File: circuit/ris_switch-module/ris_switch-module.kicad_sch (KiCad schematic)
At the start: 32 parts, among them J1 JST-PH-5P-M, J12 JST-PH-5P-F, J13 JST-PH-5P-M, J14 JST-PH-2P-F, J15 JST-PH-2P-M, J2 JST-PH-5P-M, J3 JST-B2PS-VH-M, J4 JST-PH-2P-M, J5 JST-PH-2P-M, J6 JST-PH-2P-M, J7 JST-PH-2P-M, J8 JST-PH-2P-M, J9 JST-PH-2P-M, K1 SRD-03VDC-SL-C, K2 SRD-03VDC-SL-C, K3 SRD-03VDC-SL-C, K4 SRD-03VDC-SL-C, K5 SRD-03VDC-SL-C, K6 SRD-03VDC-SL-C, Q1 BC337-40, Q2 BC337-40, Q3 BC337-40, Q4 BC337-40, Q5 BC337-40, Q6 BC337-40, U5 74HC595N_112

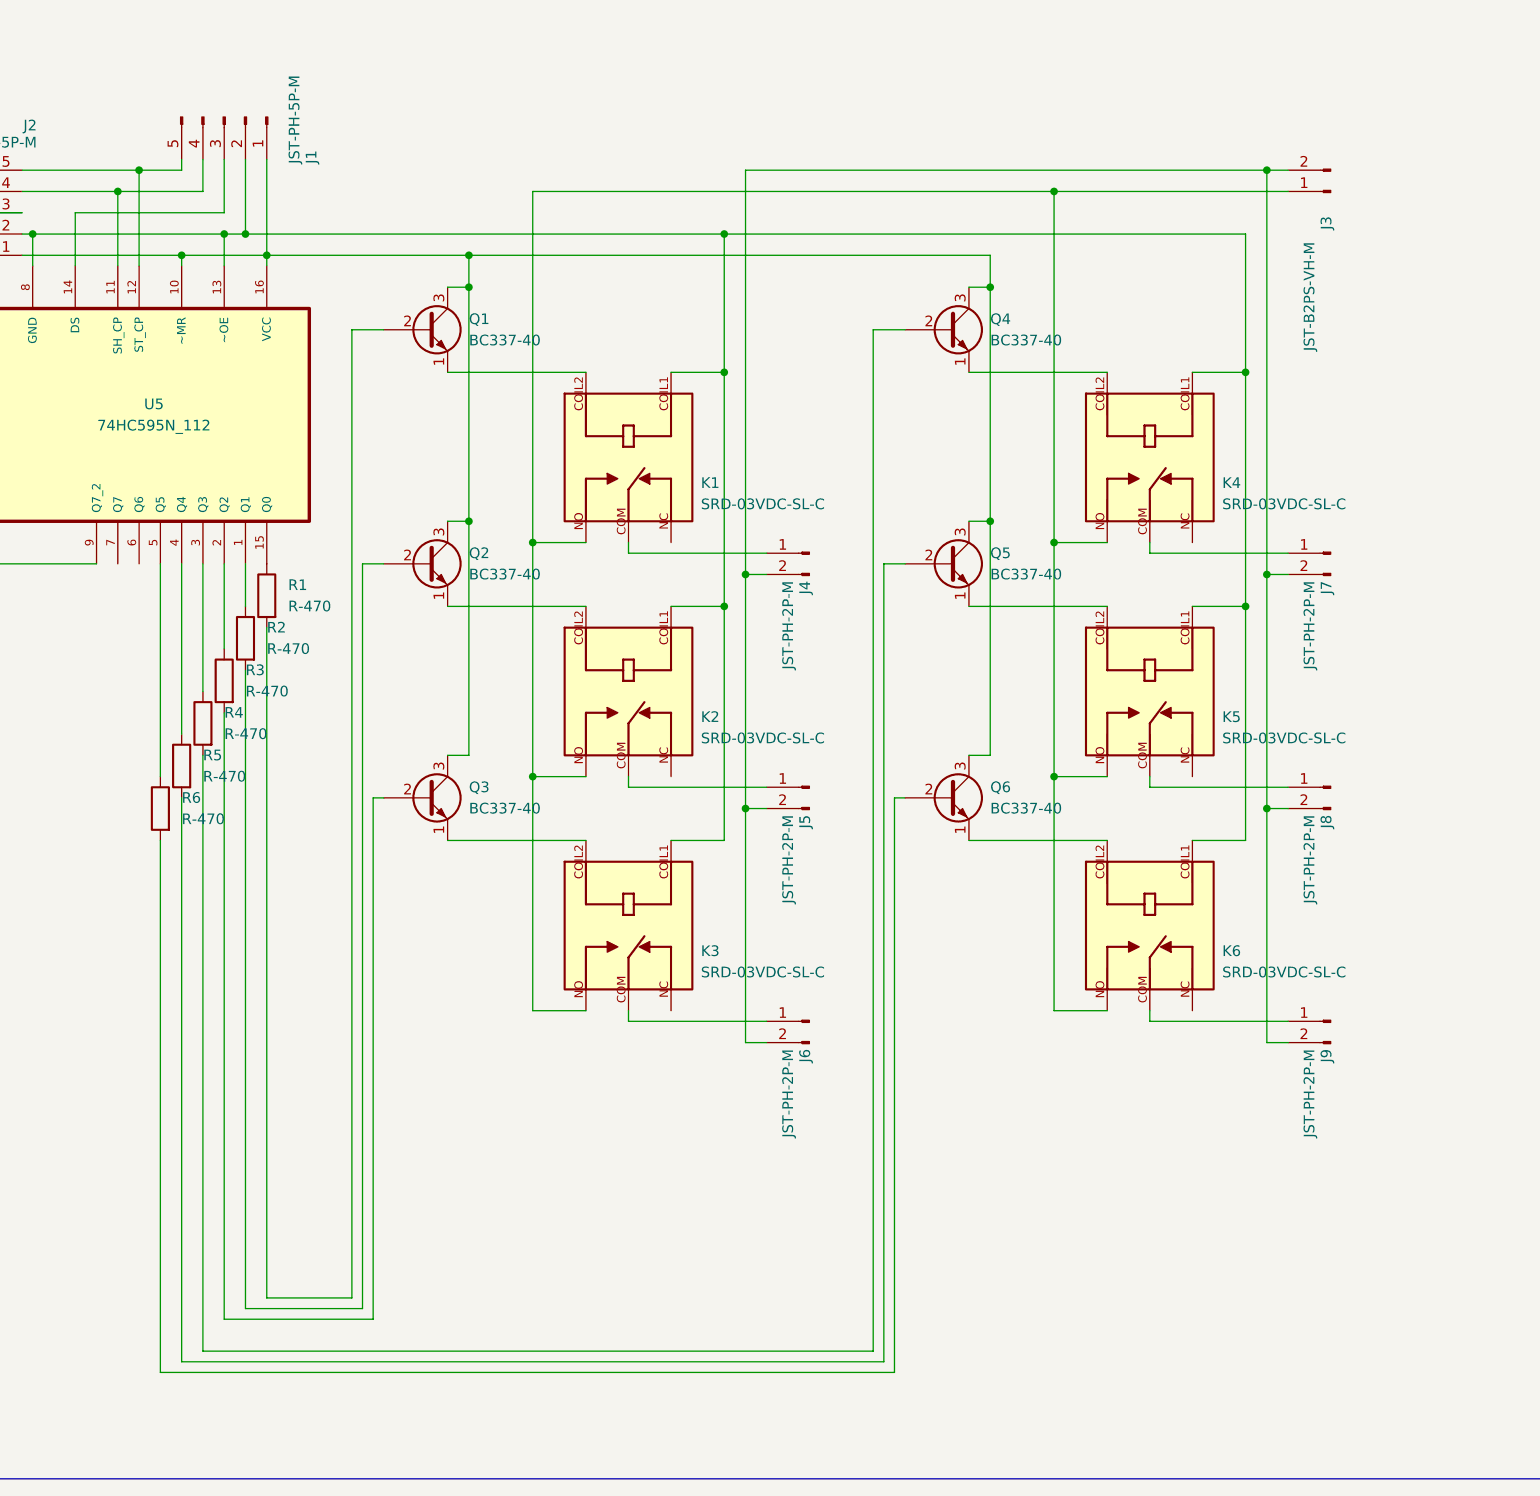
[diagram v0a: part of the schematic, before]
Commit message: Updated Circuit with Side Outputs & Mosfets
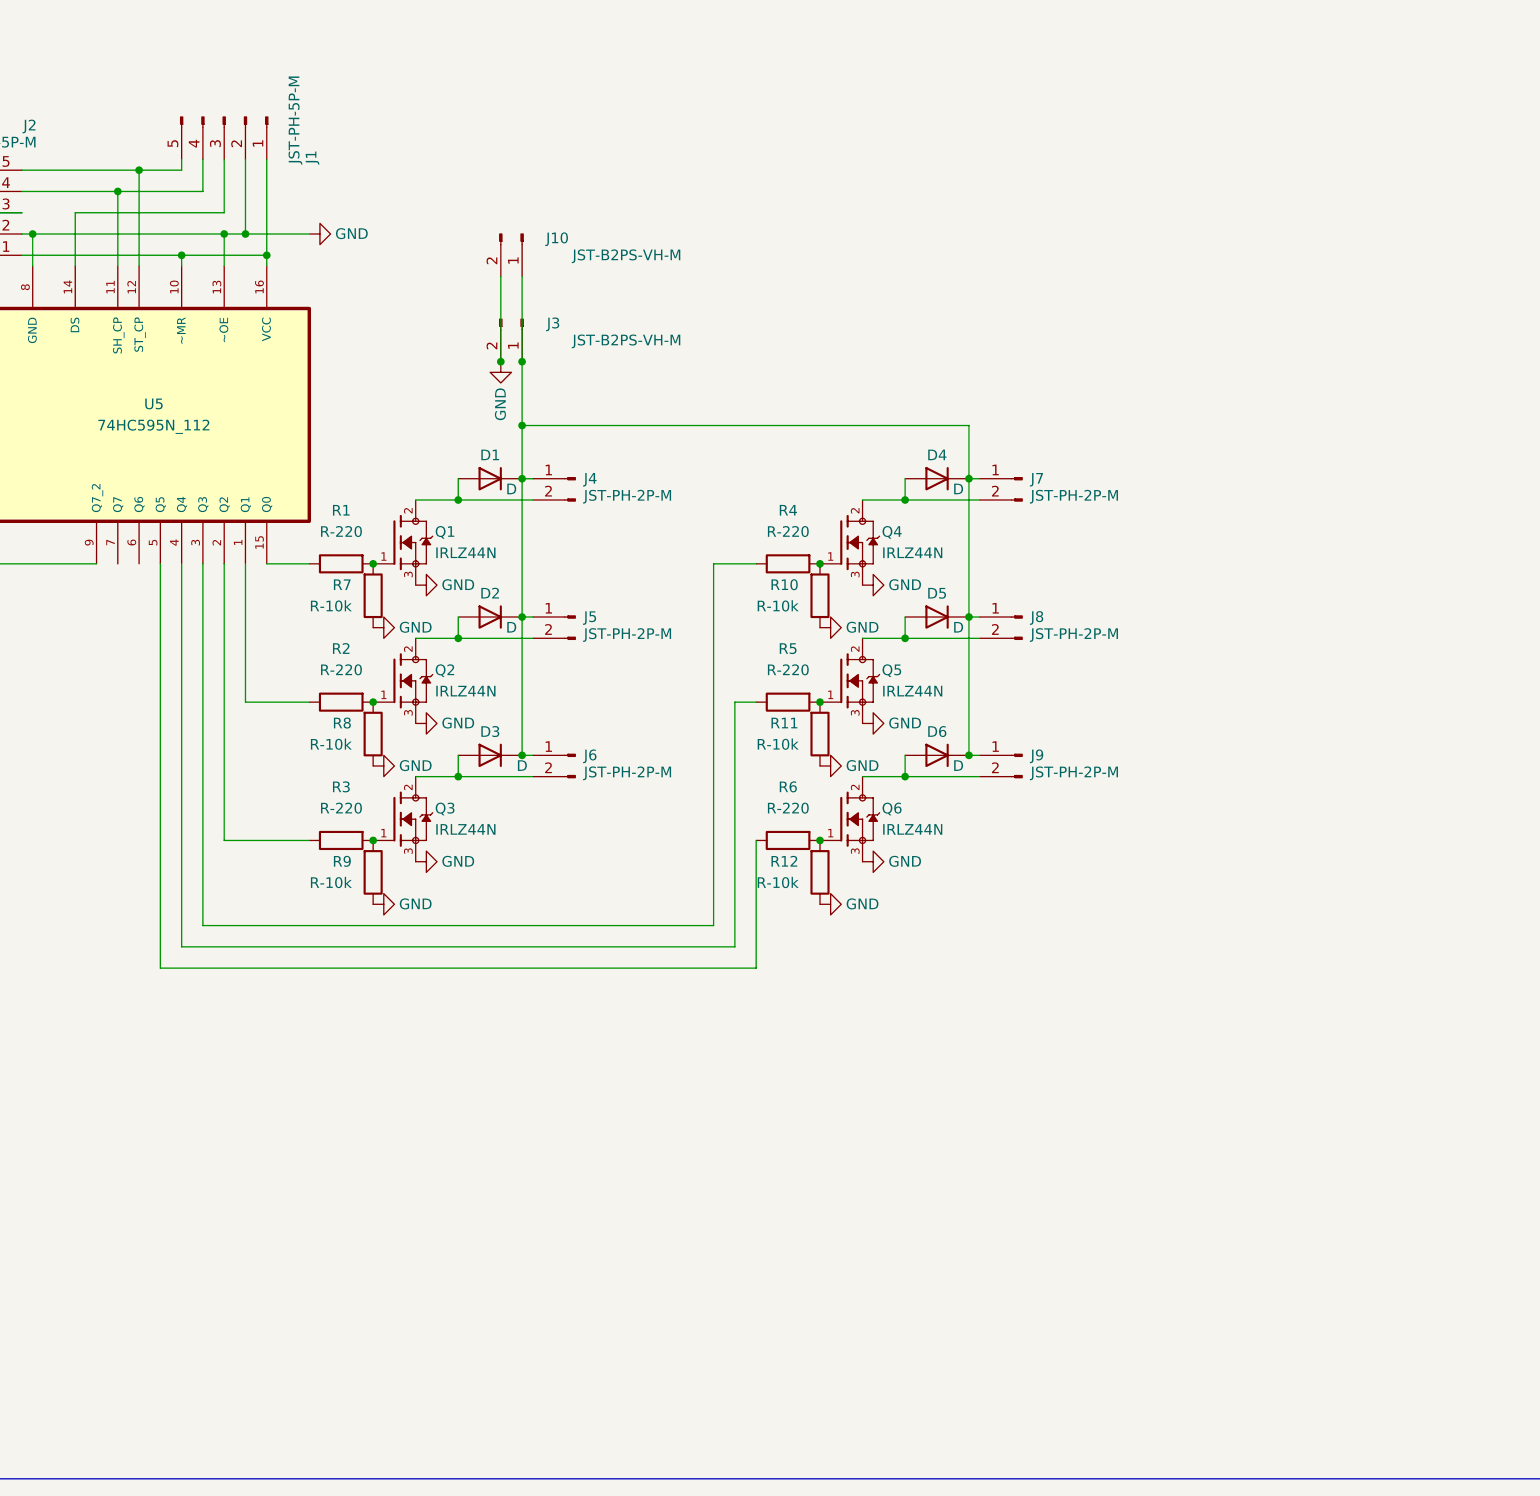
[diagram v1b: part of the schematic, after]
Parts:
- removed K1, K2, K3, K4, K5, K6: SRD-03VDC-SL-C, SRD-03VDC-SL-C:RELAY_SRD-03VDC-SL-C, symbol SRD-03VDC-SL-C:SRD-03VDC-SL-C
- removed Q1, Q2, Q3, Q4, Q5, Q6: BC337-40, 2N3904TF:TO92254P520H877-3, symbol Transistor_BJT:BC107
- added D1, D2, D3, D4, D5, D6: D, Diode_THT:D_DO-201AD_P12.70mm_Horizontal, symbol Device:D
- added J10: JST-B2PS-VH-M, JST-B2P-VH:B2P-VH, symbol Connector:Conn_01x02_Pin
- added Q1, Q2, Q3, Q4, Q5, Q6: IRLZ44N, MOSFET-IRLZ44N:TO254P1054X469X1930-3, symbol MOSFET-IRLZ44N:IRLZ44N
- added R10, R11, R12, R7, R8, R9: R-10k, Resistor_THT:R_Axial_DIN0207_L6.3mm_D2.5mm_P7.62mm_Horizontal, symbol Device:R
- J3: footprint JST-B2PS-VH:B2PS-VH -> JST-B2P-VH:B2P-VH
- R1, R2, R3, R4, R5, R6: value R-470 -> R-220
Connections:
- net at R4.2: now also Q4.1, R10.2
- net GND: now reaches J1.2 (Pin_2), J2.2 (Pin_2), U5.13 (~OE), U5.8 (GND)
- net GND: now also J3.2 (Pin_2), J10.2 (Pin_2), Q1.3, Q2.3, Q3.3, Q4.3, Q5.3, Q6.3, R10.1, R11.1, R12.1, R7.1, R8.1, R9.1
- net at J5.1 (Pin_1): now also J3.1 (Pin_1), J4.1 (Pin_1), J6.1 (Pin_1), J7.1 (Pin_1), J8.1 (Pin_1), J9.1 (Pin_1), D1.1 (K), D2.1 (K), D3.1 (K), D4.1 (K), D5.1 (K), D6.1 (K), J10.1 (Pin_1)
- net at R3.2: now also Q3.1, R9.2
- net at R2.2: now also Q2.1, R8.2
- net at R1.2: now also Q1.1, R7.2
- net at R6.2: now also Q6.1, R12.2
- net at R5.2: now also Q5.1, R11.2
- new net: D3.2 (A), J6.2 (Pin_2), Q3.2
- new net: D4.2 (A), J7.2 (Pin_2), Q4.2
- new net: D1.2 (A), J4.2 (Pin_2), Q1.2
- new net: D6.2 (A), J9.2 (Pin_2), Q6.2
- new net: D2.2 (A), J5.2 (Pin_2), Q2.2
- new net: D5.2 (A), J8.2 (Pin_2), Q5.2
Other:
- moved on the sheet: J3, J4
